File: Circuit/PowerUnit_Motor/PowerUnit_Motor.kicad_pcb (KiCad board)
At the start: 2 copper layers, 100 x 65.5 mm, 21 parts, among them J1 Conn_01x02_Pin, J10 Conn_01x02_Pin, J11 Conn_01x02_Pin, J2 Conn_01x02_Pin, J3 Conn_01x02_Pin, J4 Conn_01x02_Pin, J5 Conn_01x02_Pin, J6 Conn_01x02_Pin, J7 Conn_01x02_Pin, J8 Conn_01x02_Pin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

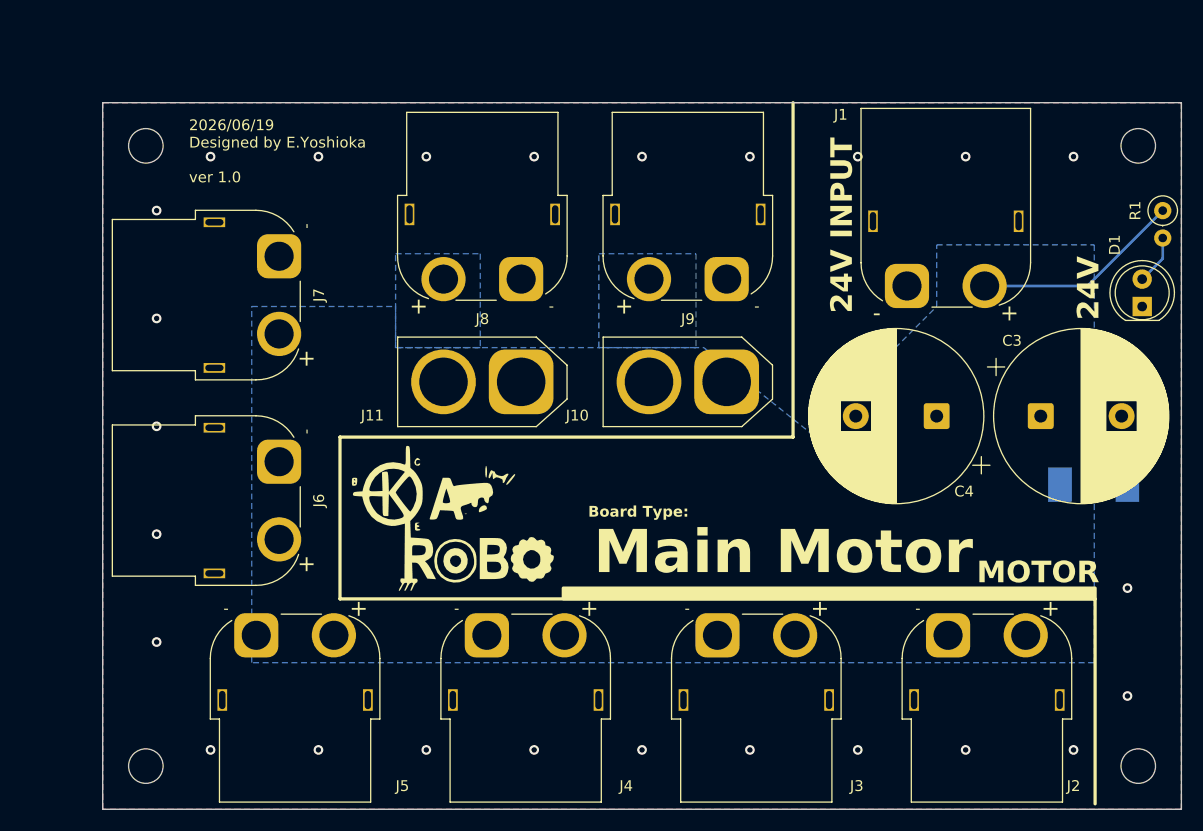
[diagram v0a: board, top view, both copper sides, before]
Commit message: YDS512F基板完成 24V基板とメインモータ基板を微修正
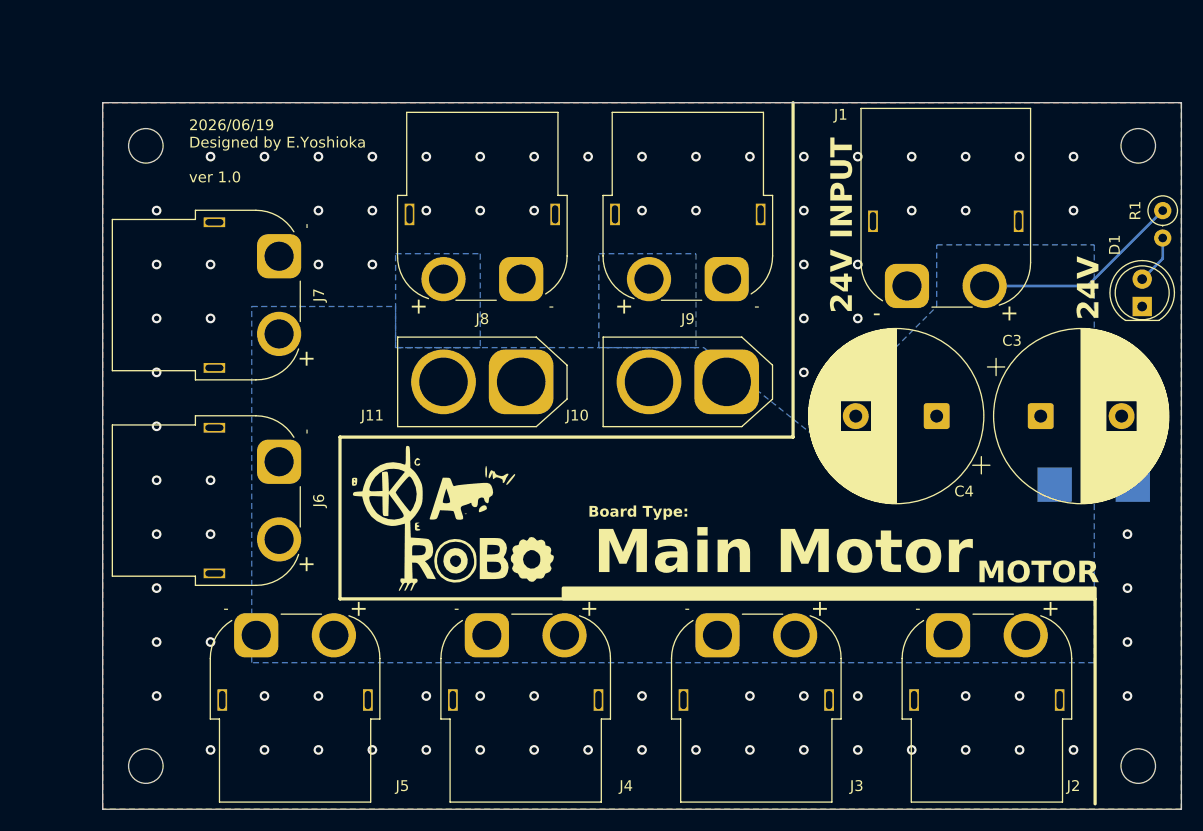
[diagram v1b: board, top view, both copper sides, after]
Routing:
- net GNDPWR: vias 25 -> 83

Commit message: サーボ基板完成
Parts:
- moved REF** 8.50 mm to (126.0, 83.0)
- moved REF** 8.50 mm to (34.0, 83.0)
- moved J6 8.35 mm to (38.0, 63.3)
- moved J7 8.35 mm to (38.0, 44.2)
- moved J8 8.35 mm to (68.8, 38.0)
- moved J9 8.35 mm to (87.8, 38.0)
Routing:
- net GNDPWR: vias 83 -> 59
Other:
- board size 100 x 65.5 mm -> 100 x 57 mm
